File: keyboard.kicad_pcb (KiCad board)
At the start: 2 copper layers, 285 x 94.6 mm, 315 parts, among them IC1 ATMEGA32U4, J1 USB_2, P1 DIL16, P2 DIL16, P3 CONN_6, SW1 SW_PUSH, X1 ASX4

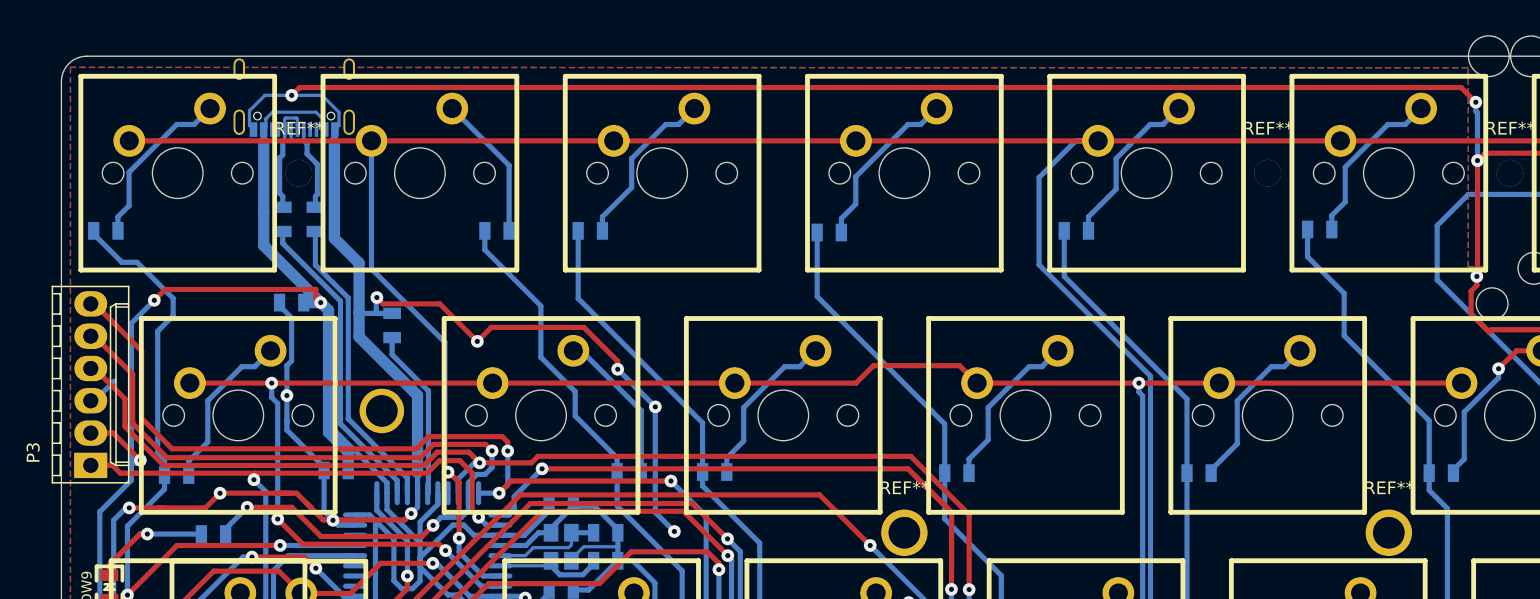
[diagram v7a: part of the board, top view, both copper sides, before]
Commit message: add ESD protector, overcurrent protector; add cc1/2 pulldown resistor
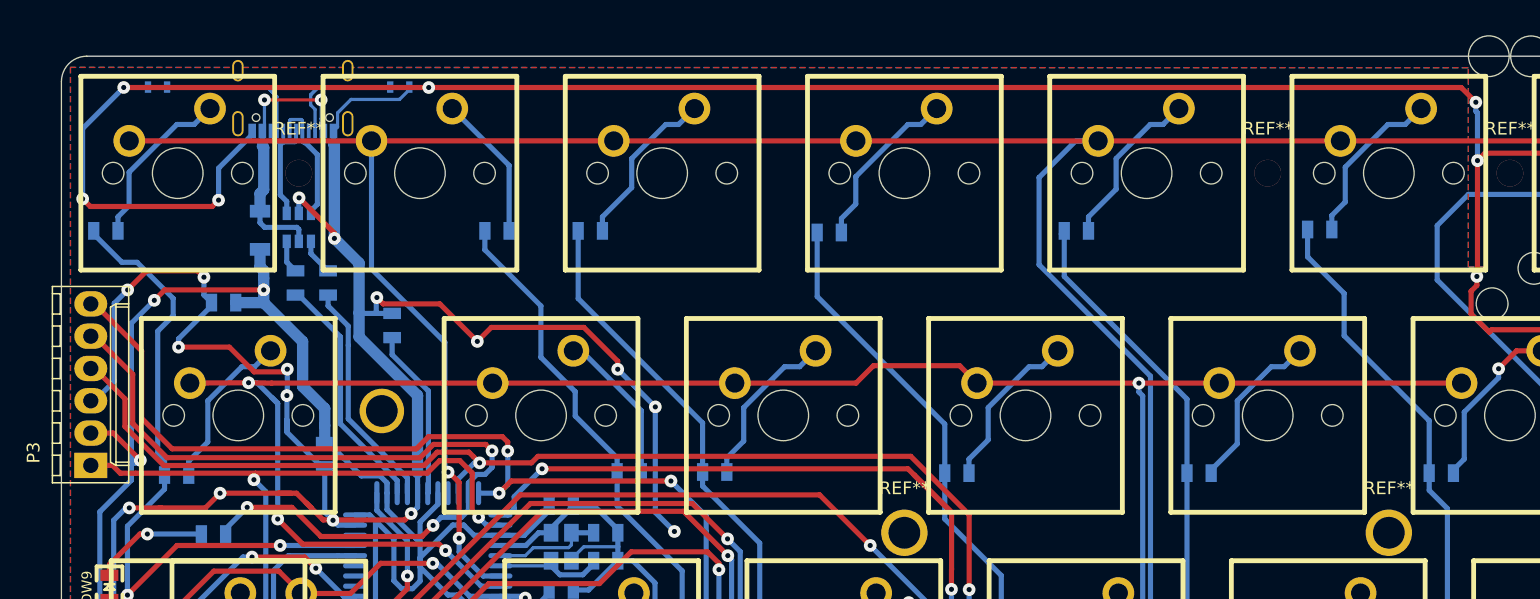
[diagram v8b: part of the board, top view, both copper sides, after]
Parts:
- added F1: FUSE, Capacitors_SMD:C_1206, B.Cu at (77.9, 78.3)
- added R1: 5.1k, Resistors_SMD:R_0603, B.Cu at (69.8, 67.0)
- added R2: 5.1k, Resistors_SMD:R_0603, B.Cu at (88.9, 67.0)
- added U1: USBLC6-2SC6, TO_SOT_Packages_SMD:SOT-23-6, B.Cu at (81.0, 78.1)
- J1: value USB_2 -> USBTYPEC
- moved C1 5.35 mm to (75.0, 84.0)
- moved R10 5.10 mm to (80.7, 82.5)
- moved R11 5.10 mm to (83.3, 82.5)
- moved C4 1.54 mm to (83.0, 96.0), turned to 270 degrees
- moved J1 0.16 mm to (80.5, 68.0)
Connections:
- J1 pad A5: (no net) -> Net-(J1-PadA5)
- J1 pad B5: (no net) -> Net-(J1-PadB5)
- R10 pad 1: Net-(J1-Pad2) -> Net-(R10-Pad1)
- R11 pad 2: Net-(J1-Pad3) -> Net-(R11-Pad2)
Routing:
- net GND: track 1345.7 -> 1418.1 mm, vias 89 -> 98
- net VCC: track 386.1 -> 362.5 mm
- net Net-(F1-Pad1): track 0.00 -> 21.1 mm, vias 0 -> 2
- net Net-(J1-PadA5): track 0.00 -> 12.2 mm
- net Net-(J1-PadA6): track 0.00 -> 10.3 mm
- net Net-(J1-PadB5): track 0.00 -> 10.2 mm
- net Net-(J1-Pad2): track 9.12 -> 0.00 mm
- net Net-(J1-PadA7): track 0.00 -> 8.81 mm
- net Net-(J1-Pad3): track 8.51 -> 0.00 mm
- net Net-(IC1-Pad4): track 23.6 -> 18.2 mm
- net Net-(IC1-Pad3): track 24.3 -> 19.0 mm
- net Net-(R11-Pad2): track 0.00 -> 2.88 mm
- net Net-(R10-Pad1): track 0.00 -> 2.60 mm
- net /row2: track 198.6 -> 200.5 mm
